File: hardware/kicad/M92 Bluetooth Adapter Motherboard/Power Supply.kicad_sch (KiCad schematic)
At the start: 32 parts, among them IC2 L7805CDT-TR, IC4 NJU7031D, IC4 TL7660IDR, J1 Conn_External_Power, J4 B2B-XH-A, J5 B2B-XH-A, J9 B6B-XH-A, K3 HE3621A1210, K4 HE3621A1210, Q2 PN2222ATA

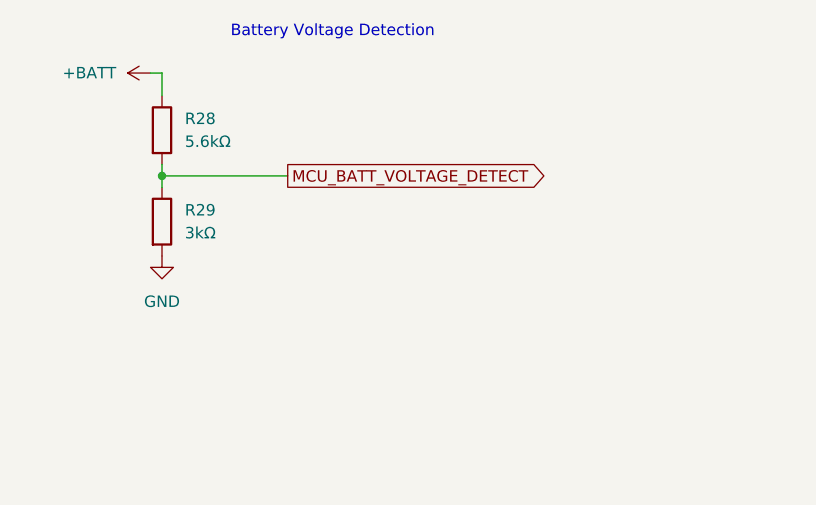
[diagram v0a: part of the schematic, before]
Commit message: Increase battery voltage divider resistor values to reduce power consumption when powered off
Increased value of battery voltage divider resistors by about 10x to reduce current draw from about 1.4 mA to about 0.13 mA. This reduces a major source of current draw when the phone is "off" and the MCU is sleeping.

Increased ADC acquisition time to account for higher impedance input (about 90k, compared to datasheet recommended max of 10k).

Added a 10nF capacitor to the ADC input pin as a "reservoir" to help charge the sample/hold cap despite the high impedance.

Adjusted min/max battery level ADC value mappings to account for change in voltage divider ratio.
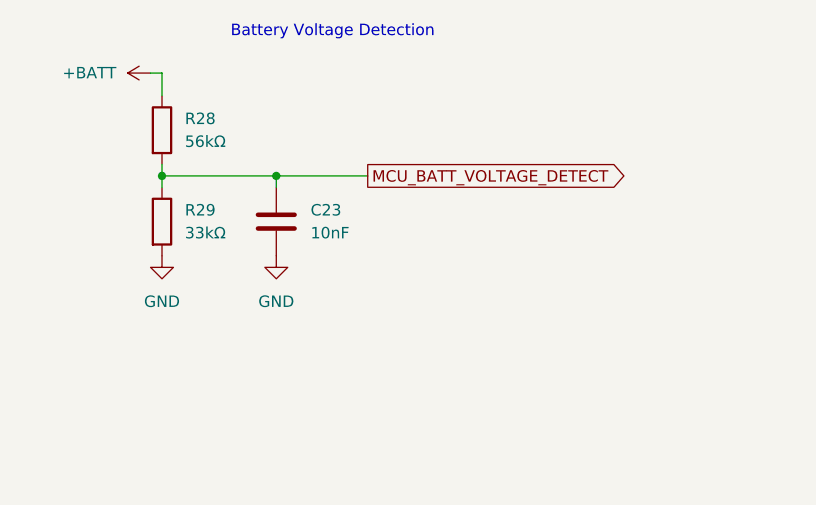
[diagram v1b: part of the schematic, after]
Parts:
- added C23: 10nF, Capacitor_SMD:C_1206_3216Metric_Pad1.33x1.80mm_HandSolder, symbol Device:C
- R28: value 5.6kΩ -> 56kΩ; JLCPCB Part # C212538 -> C137252; Manufacturer_Part_Number CR1206-FX-5601ELF -> CR1206-FX-5602ELF; Mouser Part Number 652-CR1206FX-5601ELF -> 652-CR1206FX-5602ELF; Mouser Price/Stock https://www.mouser.com/ProductDetail/Bourns/CR1206-FX-5601E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 -> https://www.mouser.com/ProductDetail/Bourns/CR1206-FX-5602E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
- R29: value 3kΩ -> 33kΩ; JLCPCB Part # C3000618 -> C229558; Manufacturer_Part_Number CR1206-FX-3001ELF -> CR1206-FX-3302ELF; Mouser Part Number 652-CR1206FX-3001ELF -> 652-CR1206FX-3302ELF; Mouser Price/Stock https://www.mouser.com/ProductDetail/Bourns/CR1206-FX-3001E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 -> https://www.mouser.com/ProductDetail/Bourns/CR1206-FX-3302E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
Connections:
- net GND: now also C23.2
- net MCU_BATT_VOLTAGE_DETECT: now also C23.1
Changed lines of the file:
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@@
   (junction (at 208.28 114.3) (diameter 0) (color 0 0 0 0)
+  )
+  (junction (at 223.52 43.18) (diameter 0) (color 0 0 0 0)
   )
   (no_connect (at 59.69 45.72))
@@
     (stroke (width 0) (type default))
   )
-  (wire (pts (xy 210.82 43.18) (xy 224.79 43.18))
+  (wire (pts (xy 210.82 43.18) (xy 223.52 43.18))
     (stroke (width 0) (type default))
   )
@@
     (stroke (width 0) (type default))
   )
+  (wire (pts (xy 223.52 44.45) (xy 223.52 43.18))
+    (stroke (width 0) (type default))
+  )
   (wire (pts (xy 256.54 111.76) (xy 261.62 111.76))
     (stroke (width 0) (type default))
@@
   )
   (wire (pts (xy 256.54 119.38) (xy 251.46 119.38))
+    (stroke (width 0) (type default))
+  )
+  (wire (pts (xy 223.52 43.18) (xy 233.68 43.18))
     (stroke (width 0) (type default))
   )
@@
     )
   )
-  (global_label "MCU_BATT_VOLTAGE_DETECT" (shape output) (at 224.79 43.18 0) (fields_autoplaced)
+  (global_label "MCU_BATT_VOLTAGE_DETECT" (shape output) (at 233.68 43.18 0) (fields_autoplaced)
     (effects (font (size 1.27 1.27)) (justify left))
-    (property "Intersheetrefs" "${INTERSHEET_REFS}" (at 253.7193 43.18 0)
+    (property "Intersheetrefs" "${INTERSHEET_REFS}" (at 262.6093 43.18 0)
       (effects (font (size 1.27 1.27)) (justify left))
     )
@@
     )
   )
+  (symbol (lib_id "power:GND") (at 223.52 52.07 0) (unit 1)
+    (in_bom yes) (on_board yes) (dnp no) (fields_autoplaced)
+    (property "Reference" "#PWR010" (at 223.52 58.42 0)
+      (effects (font (size 1.27 1.27)) hide)
+    )
+    (property "Value" "GND" (at 223.52 57.15 0)
+      (effects (font (size 1.27 1.27)))
+    )
+    (property "Footprint" "" (at 223.52 52.07 0)
+      (effects (font (size 1.27 1.27)) hide)
+    )
+    (property "Datasheet" "" (at 223.52 52.07 0)
+      (effects (font (size 1.27 1.27)) hide)
+    )
+    (pin "1")
+    (instances
+      (project "M92 Bluetooth Adapter Motherboard"
+        (path "/d695ac67-4f6c-46c1-9ce6-2d543d3b66ce"
+          (reference "#PWR010") (unit 1)
+        )
+        (path "/d695ac67-4f6c-46c1-9ce6-2d543d3b66ce/a56585ec-fbf3-4835-9390-a703fb925d02"
+          (reference "#PWR050") (unit 1)
+        )
+        (path "/d695ac67-4f6c-46c1-9ce6-2d543d3b66ce/8852b3cd-e5e9-4a63-b614-38055f92a00c"
+          (reference "#PWR010") (unit 1)
+        )
+      )
+    )
+  )
   (symbol (lib_id "power:GND") (at 71.12 102.87 90) (unit 1)
     (in_bom yes) (on_board yes) (dnp no) (fields_autoplaced)
@@
       (effects (font (size 1.27 1.27)) (justify left))
     )
-    (property "Value" "3kΩ" (at 213.36 49.53 0)
+    (property "Value" "33kΩ" (at 213.36 49.53 0)
       (effects (font (size 1.27 1.27)) (justify left))
     )
@@
       (effects (font (size 1.27 1.27)) hide)
     )
-    (property "Manufacturer_Part_Number" "CR1206-FX-3001ELF" (at 210.82 48.26 0)
-      (effects (font (size 1.27 1.27)) hide)
-    )
-    (property "Mouser Part Number" "652-CR1206FX-3001ELF" (at 210.82 48.26 0)
-      (effects (font (size 1.27 1.27)) hide)
-    )
-    (property "Mouser Price/Stock" "https://www.mouser.com/ProductDetail/Bourns/CR1206-FX-3001ELF?qs=raSpJxvwqHExN1%252BFFpcSkA%3D%3D" (at 210.82 48.26 0)
-      (effects (font (size 1.27 1.27)) hide)
-    )
-    (property "JLCPCB Part #" "C3000618" (at 210.82 48.26 0)
+    (property "Manufacturer_Part_Number" "CR1206-FX-3302ELF" (at 210.82 48.26 0)
+      (effects (font (size 1.27 1.27)) hide)
+    )
+    (property "Mouser Part Number" "652-CR1206FX-3302ELF" (at 210.82 48.26 0)
+      (effects (font (size 1.27 1.27)) hide)
+    )
+    (property "Mouser Price/Stock" "https://www.mouser.com/ProductDetail/Bourns/CR1206-FX-3302ELF?qs=raSpJxvwqHGlFcROEsp6ag%3D%3D" (at 210.82 48.26 0)
+      (effects (font (size 1.27 1.27)) hide)
+    )
+    (property "JLCPCB Part #" "C229558" (at 210.82 48.26 0)
       (effects (font (size 1.27 1.27)) hide)
     )
@@
         (path "/d695ac67-4f6c-46c1-9ce6-2d543d3b66ce/8852b3cd-e5e9-4a63-b614-38055f92a00c"
           (reference "R10") (unit 1)
+        )
+      )
+    )
+  )
+  (symbol (lib_id "Device:C") (at 223.52 48.26 0) (unit 1)
+    (in_bom yes) (on_board yes) (dnp no) (fields_autoplaced)
+    (property "Reference" "C23" (at 227.33 46.99 0)
+      (effects (font (size 1.27 1.27)) (justify left))
+    )
+    (property "Value" "10nF" (at 227.33 49.53 0)
+      (effects (font (size 1.27 1.27)) (justify left))
+    )
+    (property "Footprint" "Capacitor_SMD:C_1206_3216Metric_Pad1.33x1.80mm_HandSolder" (at 224.4852 52.07 0)
+      (effects (font (size 1.27 1.27)) hide)
+    )
+    (property "Datasheet" "~" (at 223.52 48.26 0)
+      (effects (font (size 1.27 1.27)) hide)
+    )
+    (property "JLCPCB Part #" "C5137623" (at 223.52 48.26 0)
+      (effects (font (size 1.27 1.27)) hide)
+    )
+    (property "Manufacturer_Name" "KEMET" (at 223.52 48.26 0)
+      (effects (font (size 1.27 1.27)) hide)
+    )
+    (property "Manufacturer_Part_Number" "C1206C103J4HACTU" (at 223.52 48.26 0)
+      (effects (font (size 1.27 1.27)) hide)
+    )
+    (property "Mouser Part Number" "80-C1206C103J4HACTU" (at 223.52 48.26 0)
+      (effects (font (size 1.27 1.27)) hide)
+    )
+    (property "Mouser Price/Stock" "https://www.mouser.com/ProductDetail/KEMET/C1206C103J4HACTU?qs=W0yvOO0ixfHuR59Cq5E7Zg%3D%3D" (at 223.52 48.26 0)
+      (effects (font (size 1.27 1.27)) hide)
+    )
+    (pin "2")
+    (pin "1")
+    (instances
+      (project "M92 Bluetooth Adapter Motherboard"
+        (path "/d695ac67-4f6c-46c1-9ce6-2d543d3b66ce/8852b3cd-e5e9-4a63-b614-38055f92a00c"
+          (reference "C23") (unit 1)
         )
       )
@@
       (effects (font (size 1.27 1.27)) (justify left))
     )
-    (property "Value" "5.6kΩ" (at 213.36 39.37 0)
+    (property "Value" "56kΩ" (at 213.36 39.37 0)
       (effects (font (size 1.27 1.27)) (justify left))
     )
@@
       (effects (font (size 1.27 1.27)) hide)
     )
-    (property "Manufacturer_Part_Number" "CR1206-FX-5601ELF" (at 210.82 38.1 0)
-      (effects (font (size 1.27 1.27)) hide)
-    )
-    (property "Mouser Part Number" "652-CR1206FX-5601ELF" (at 210.82 38.1 0)
-      (effects (font (size 1.27 1.27)) hide)
-    )
-    (property "Mouser Price/Stock" "https://www.mouser.com/ProductDetail/Bourns/CR1206-FX-5601ELF?qs=O4EQhShwvrpLgyNoO%2FwM5Q%3D%3D" (at 210.82 38.1 0)
-      (effects (font (size 1.27 1.27)) hide)
-    )
-    (property "JLCPCB Part #" "C212538" (at 210.82 38.1 0)
-      (effects (font (size 1.27 1.27)) hide)
-    )
+    (property "Manufacturer_Part_Number" "CR1206-FX-5602ELF" (at 210.82 38.1 0)
+      (effects (font (size 1.27 1.27)) hide)
+    )
+    (property "Mouser Part Number" "652-CR1206FX-5602ELF" (at 210.82 38.1 0)
+      (effects (font (size 1.27 1.27)) hide)
+    )
+    (property "Mouser Price/Stock" "https://www.mouser.com/ProductDetail/Bourns/CR1206-FX-5602ELF?qs=O4EQhShwvrpmr2Gk5hEGIw%3D%3D" (at 210.82 38.1 0)
+      (effects (font (size 1.27 1.27)) hide)
+    )
+    (property "JLCPCB Part #" "C137252" (at 210.82 38.1 0)
+      (effects (font (size 1.27 1.27)) hide)
+    )

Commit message: Update battery voltage divider to use larger resistor values
Increase voltage divider resistor values to reduce current draw.  Since I am never switching ADC input pins on the MCU and sampling rate is very low (once per 5 seconds), the very high impedance does not appear to impact ADC reading accuracy. I also found that the 10nF capacitor was unnecessary, so that is now removed.

Also updated JLCPCB part numbers for several resistors and capacitors to use "basic" parts instead of "extended" parts.
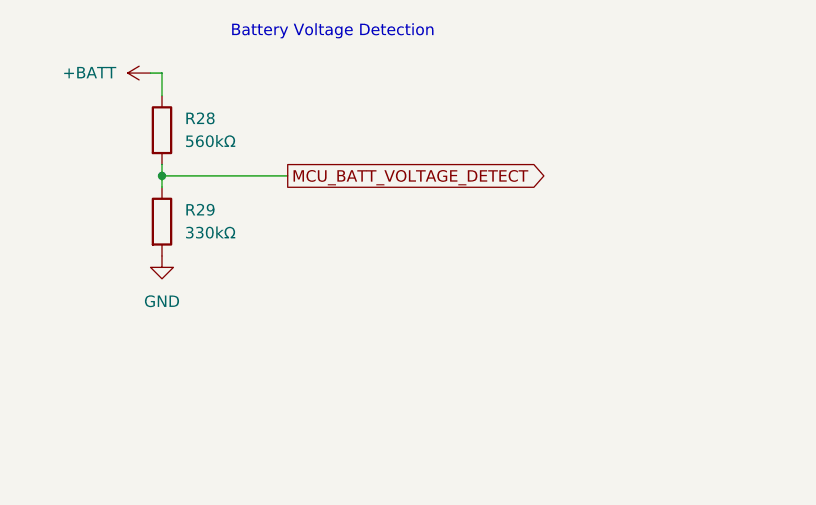
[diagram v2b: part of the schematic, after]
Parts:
- removed C23: 10nF, Capacitor_SMD:C_1206_3216Metric_Pad1.33x1.80mm_HandSolder, symbol Device:C
- C5, C6: JLCPCB Part # C5137650 -> C24497
- R26, R27, R7, R8: JLCPCB Part # C212480 -> C17900
- R28: value 56kΩ -> 560kΩ; JLCPCB Part # C137252 -> C286669; Manufacturer_Part_Number CR1206-FX-5602ELF -> CR1206-FX-5603ELF; Mouser Part Number 652-CR1206FX-5602ELF -> 652-CR1206FX-5603ELF; Mouser Price/Stock https://www.mouser.com/ProductDetail/Bourns/CR1206-FX-5602E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 -> https://www.mouser.com/ProductDetail/Bourns/CR1206-FX-5603E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
- R29: value 33kΩ -> 330kΩ; JLCPCB Part # C229558 -> C491352; Manufacturer_Part_Number CR1206-FX-3302ELF -> CR1206-FX-3303ELF; Mouser Part Number 652-CR1206FX-3302ELF -> 652-CR1206FX-3303ELF; Mouser Price/Stock https://www.mouser.com/ProductDetail/Bourns/CR1206-FX-3302E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 -> https://www.mouser.com/ProductDetail/Bourns/CR1206-FX-3303E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
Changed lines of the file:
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@@
   (junction (at 208.28 114.3) (diameter 0) (color 0 0 0 0)
-  )
-  (junction (at 223.52 43.18) (diameter 0) (color 0 0 0 0)
   )
   (no_connect (at 59.69 45.72))
@@
     (stroke (width 0) (type default))
   )
-  (wire (pts (xy 210.82 43.18) (xy 223.52 43.18))
+  (wire (pts (xy 210.82 43.18) (xy 224.79 43.18))
     (stroke (width 0) (type default))
   )
@@
     (stroke (width 0) (type default))
   )
-  (wire (pts (xy 223.52 44.45) (xy 223.52 43.18))
-    (stroke (width 0) (type default))
-  )
   (wire (pts (xy 256.54 111.76) (xy 261.62 111.76))
     (stroke (width 0) (type default))
@@
   )
   (wire (pts (xy 256.54 119.38) (xy 251.46 119.38))
-    (stroke (width 0) (type default))
-  )
-  (wire (pts (xy 223.52 43.18) (xy 233.68 43.18))
     (stroke (width 0) (type default))
   )
@@
     )
   )
-  (global_label "MCU_BATT_VOLTAGE_DETECT" (shape output) (at 233.68 43.18 0) (fields_autoplaced)
+  (global_label "MCU_BATT_VOLTAGE_DETECT" (shape output) (at 224.79 43.18 0) (fields_autoplaced)
     (effects (font (size 1.27 1.27)) (justify left))
-    (property "Intersheetrefs" "${INTERSHEET_REFS}" (at 262.6093 43.18 0)
+    (property "Intersheetrefs" "${INTERSHEET_REFS}" (at 253.7193 43.18 0)
       (effects (font (size 1.27 1.27)) (justify left))
     )
@@
       (effects (font (size 1.27 1.27)) hide)
     )
-    (property "JLCPCB Part #" "C212480" (at 34.29 44.45 0)
+    (property "JLCPCB Part #" "C17900" (at 34.29 44.45 0)
       (effects (font (size 1.27 1.27)) hide)
     )
@@
       (effects (font (size 1.27 1.27)) hide)
     )
-    (property "JLCPCB Part #" "C5137650" (at 96.52 163.83 0)
+    (property "JLCPCB Part #" "C24497" (at 96.52 163.83 0)
       (effects (font (size 1.27 1.27)) hide)
     )
@@
       (effects (font (size 1.27 1.27)) hide)
     )
-    (property "JLCPCB Part #" "C5137650" (at 39.37 111.76 0)
+    (property "JLCPCB Part #" "C24497" (at 39.37 111.76 0)
       (effects (font (size 1.27 1.27)) hide)
     )
@@
         (path "/d695ac67-4f6c-46c1-9ce6-2d543d3b66ce/8852b3cd-e5e9-4a63-b614-38055f92a00c"
           (reference "C8") (unit 1)
-        )
-      )
-    )
-  )
-  (symbol (lib_id "power:GND") (at 223.52 52.07 0) (unit 1)
-    (in_bom yes) (on_board yes) (dnp no) (fields_autoplaced)
-    (property "Reference" "#PWR010" (at 223.52 58.42 0)
-      (effects (font (size 1.27 1.27)) hide)
-    )
-    (property "Value" "GND" (at 223.52 57.15 0)
-      (effects (font (size 1.27 1.27)))
-    )
-    (property "Footprint" "" (at 223.52 52.07 0)
-      (effects (font (size 1.27 1.27)) hide)
-    )
-    (property "Datasheet" "" (at 223.52 52.07 0)
-      (effects (font (size 1.27 1.27)) hide)
-    )
-    (pin "1")
-    (instances
-      (project "M92 Bluetooth Adapter Motherboard"
-        (path "/d695ac67-4f6c-46c1-9ce6-2d543d3b66ce"
-          (reference "#PWR010") (unit 1)
-        )
-        (path "/d695ac67-4f6c-46c1-9ce6-2d543d3b66ce/a56585ec-fbf3-4835-9390-a703fb925d02"
-          (reference "#PWR050") (unit 1)
-        )
-        (path "/d695ac67-4f6c-46c1-9ce6-2d543d3b66ce/8852b3cd-e5e9-4a63-b614-38055f92a00c"
-          (reference "#PWR010") (unit 1)
         )
       )
@@
       (effects (font (size 1.27 1.27)) hide)
     )
-    (property "JLCPCB Part #" "C5137650" (at 256.54 105.41 0)
+    (property "JLCPCB Part #" "C24497" (at 256.54 105.41 0)
       (effects (font (size 1.27 1.27)) hide)
     )
@@
       (effects (font (size 1.27 1.27)) hide)
     )
-    (property "JLCPCB Part #" "C212480" (at 104.14 48.26 0)
+    (property "JLCPCB Part #" "C17900" (at 104.14 48.26 0)
       (effects (font (size 1.27 1.27)) hide)
     )
@@
       (effects (font (size 1.27 1.27)) (justify left))
     )
-    (property "Value" "33kΩ" (at 213.36 49.53 0)
+    (property "Value" "330kΩ" (at 213.36 49.53 0)
       (effects (font (size 1.27 1.27)) (justify left))
     )
@@
       (effects (font (size 1.27 1.27)) hide)
     )
-    (property "Manufacturer_Part_Number" "CR1206-FX-3302ELF" (at 210.82 48.26 0)
-      (effects (font (size 1.27 1.27)) hide)
-    )
-    (property "Mouser Part Number" "652-CR1206FX-3302ELF" (at 210.82 48.26 0)
-      (effects (font (size 1.27 1.27)) hide)
-    )
-    (property "Mouser Price/Stock" "https://www.mouser.com/ProductDetail/Bourns/CR1206-FX-3302ELF?qs=raSpJxvwqHGlFcROEsp6ag%3D%3D" (at 210.82 48.26 0)
-      (effects (font (size 1.27 1.27)) hide)
-    )
-    (property "JLCPCB Part #" "C229558" (at 210.82 48.26 0)
+    (property "Manufacturer_Part_Number" "CR1206-FX-3303ELF" (at 210.82 48.26 0)
+      (effects (font (size 1.27 1.27)) hide)
+    )
+    (property "Mouser Part Number" "652-CR1206FX-3303ELF" (at 210.82 48.26 0)
+      (effects (font (size 1.27 1.27)) hide)
+    )
+    (property "Mouser Price/Stock" "https://www.mouser.com/ProductDetail/Bourns/CR1206-FX-3303ELF?qs=raSpJxvwqHE5WwCUcAsRuA%3D%3D" (at 210.82 48.26 0)
+      (effects (font (size 1.27 1.27)) hide)
+    )
+    (property "JLCPCB Part #" "C491352" (at 210.82 48.26 0)
       (effects (font (size 1.27 1.27)) hide)
     )
@@
       (effects (font (size 1.27 1.27)) hide)
     )
-    (property "JLCPCB Part #" "C212480" (at 195.58 119.38 0)
+    (property "JLCPCB Part #" "C17900" (at 195.58 119.38 0)
       (effects (font (size 1.27 1.27)) hide)
     )
@@
         (path "/d695ac67-4f6c-46c1-9ce6-2d543d3b66ce/8852b3cd-e5e9-4a63-b614-38055f92a00c"
           (reference "R10") (unit 1)
-        )
-      )
-    )
-  )
-  (symbol (lib_id "Device:C") (at 223.52 48.26 0) (unit 1)
-    (in_bom yes) (on_board yes) (dnp no) (fields_autoplaced)
-    (property "Reference" "C23" (at 227.33 46.99 0)
-      (effects (font (size 1.27 1.27)) (justify left))
-    )
-    (property "Value" "10nF" (at 227.33 49.53 0)
-      (effects (font (size 1.27 1.27)) (justify left))
-    )
-    (property "Footprint" "Capacitor_SMD:C_1206_3216Metric_Pad1.33x1.80mm_HandSolder" (at 224.4852 52.07 0)
-      (effects (font (size 1.27 1.27)) hide)
-    )
-    (property "Datasheet" "~" (at 223.52 48.26 0)
-      (effects (font (size 1.27 1.27)) hide)
-    )
-    (property "JLCPCB Part #" "C5137623" (at 223.52 48.26 0)
-      (effects (font (size 1.27 1.27)) hide)
-    )
-    (property "Manufacturer_Name" "KEMET" (at 223.52 48.26 0)
-      (effects (font (size 1.27 1.27)) hide)
-    )
-    (property "Manufacturer_Part_Number" "C1206C103J4HACTU" (at 223.52 48.26 0)
-      (effects (font (size 1.27 1.27)) hide)
-    )
-    (property "Mouser Part Number" "80-C1206C103J4HACTU" (at 223.52 48.26 0)
-      (effects (font (size 1.27 1.27)) hide)
-    )
-    (property "Mouser Price/Stock" "https://www.mouser.com/ProductDetail/KEMET/C1206C103J4HACTU?qs=W0yvOO0ixfHuR59Cq5E7Zg%3D%3D" (at 223.52 48.26 0)
-      (effects (font (size 1.27 1.27)) hide)
-    )
-    (pin "2")
-    (pin "1")
-    (instances
-      (project "M92 Bluetooth Adapter Motherboard"
-        (path "/d695ac67-4f6c-46c1-9ce6-2d543d3b66ce/8852b3cd-e5e9-4a63-b614-38055f92a00c"
-          (reference "C23") (unit 1)
         )
       )
@@
       (effects (font (size 1.27 1.27)) (justify left))
     )
-    (property "Value" "56kΩ" (at 213.36 39.37 0)
+    (property "Value" "560kΩ" (at 213.36 39.37 0)
       (effects (font (size 1.27 1.27)) (justify left))
     )
@@
       (effects (font (size 1.27 1.27)) hide)
     )
-    (property "Manufacturer_Part_Number" "CR1206-FX-5602ELF" (at 210.82 38.1 0)
-      (effects (font (size 1.27 1.27)) hide)
-    )
-    (property "Mouser Part Number" "652-CR1206FX-5602ELF" (at 210.82 38.1 0)
-      (effects (font (size 1.27 1.27)) hide)
-    )
-    (property "Mouser Price/Stock" "https://www.mouser.com/ProductDetail/Bourns/CR1206-FX-5602ELF?qs=O4EQhShwvrpmr2Gk5hEGIw%3D%3D" (at 210.82 38.1 0)
-      (effects (font (size 1.27 1.27)) hide)
-    )
-    (property "JLCPCB Part #" "C137252" (at 210.82 38.1 0)
+    (property "Manufacturer_Part_Number" "CR1206-FX-5603ELF" (at 210.82 38.1 0)
+      (effects (font (size 1.27 1.27)) hide)
+    )
+    (property "Mouser Part Number" "652-CR1206FX-5603ELF" (at 210.82 38.1 0)
+      (effects (font (size 1.27 1.27)) hide)
+    )
+    (property "Mouser Price/Stock" "https://www.mouser.com/ProductDetail/Bourns/CR1206-FX-5603ELF?qs=O4EQhShwvro3dlk2jEyADg%3D%3D" (at 210.82 38.1 0)
+      (effects (font (size 1.27 1.27)) hide)
+    )
+    (property "JLCPCB Part #" "C286669" (at 210.82 38.1 0)
       (effects (font (size 1.27 1.27)) hide)
     )
@@
       (effects (font (size 1.27 1.27)) hide)
     )
-    (property "JLCPCB Part #" "C212480" (at 195.58 109.22 0)
-      (effects (font (size 1.27 1.27)) hide)
-    )
+    (property "JLCPCB Part #" "C17900" (at 195.58 109.22 0)
+      (effects (font (size 1.27 1.27)) hide)
+    )
